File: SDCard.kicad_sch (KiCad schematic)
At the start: 3 parts, among them J1 Micro_SD_Card_Det1, U1 rv1126/rv1109

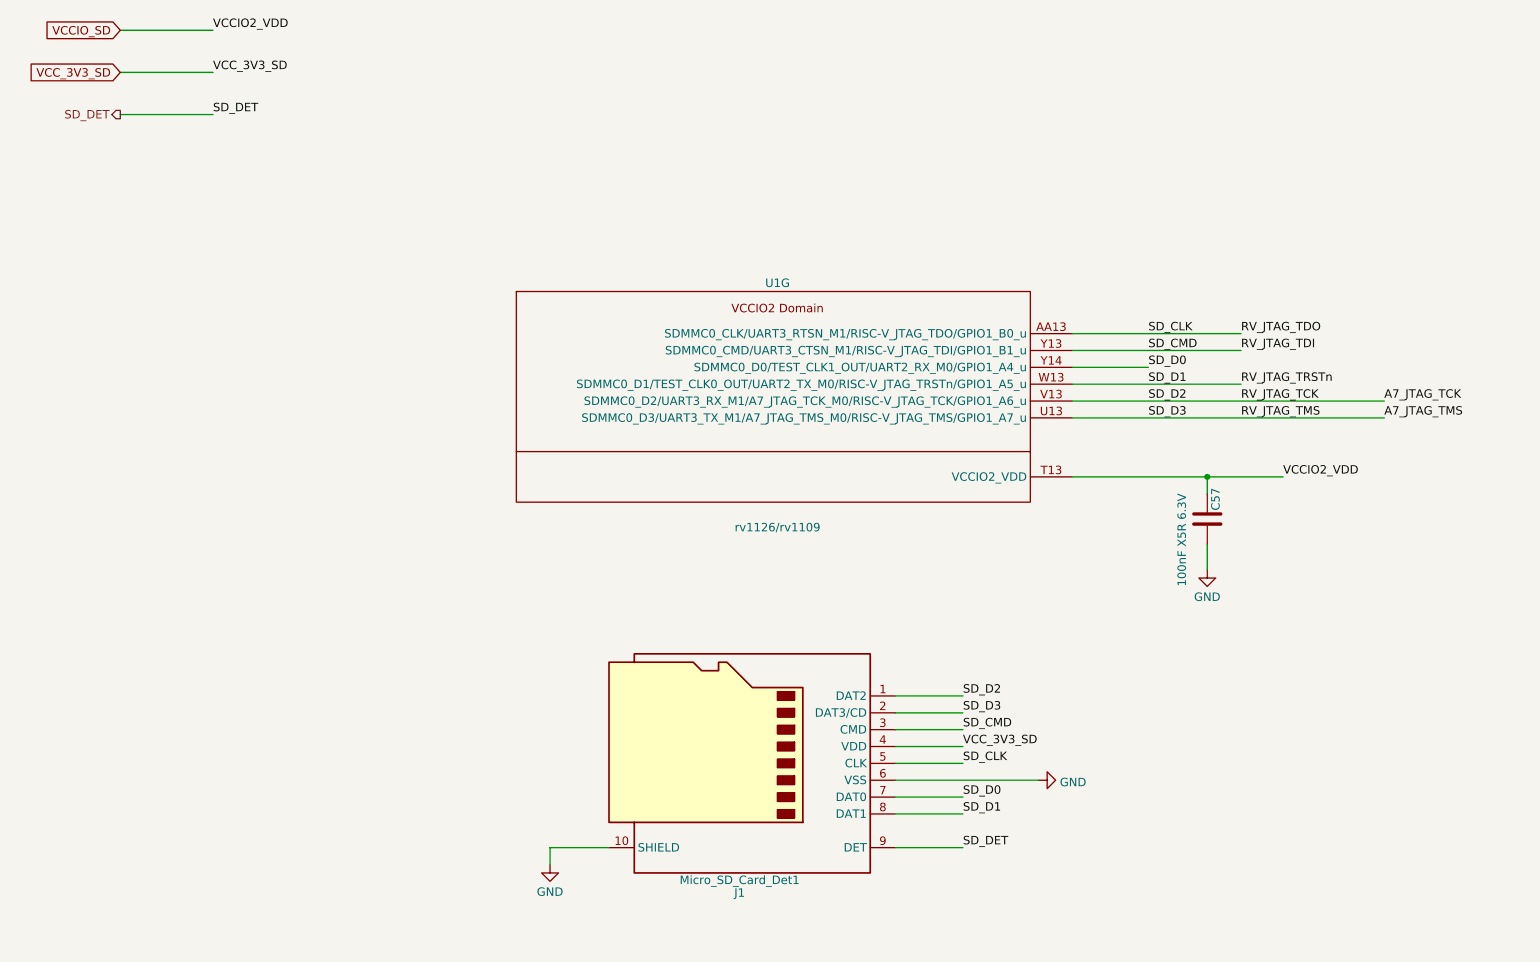
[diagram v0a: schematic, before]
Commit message: added SDCard
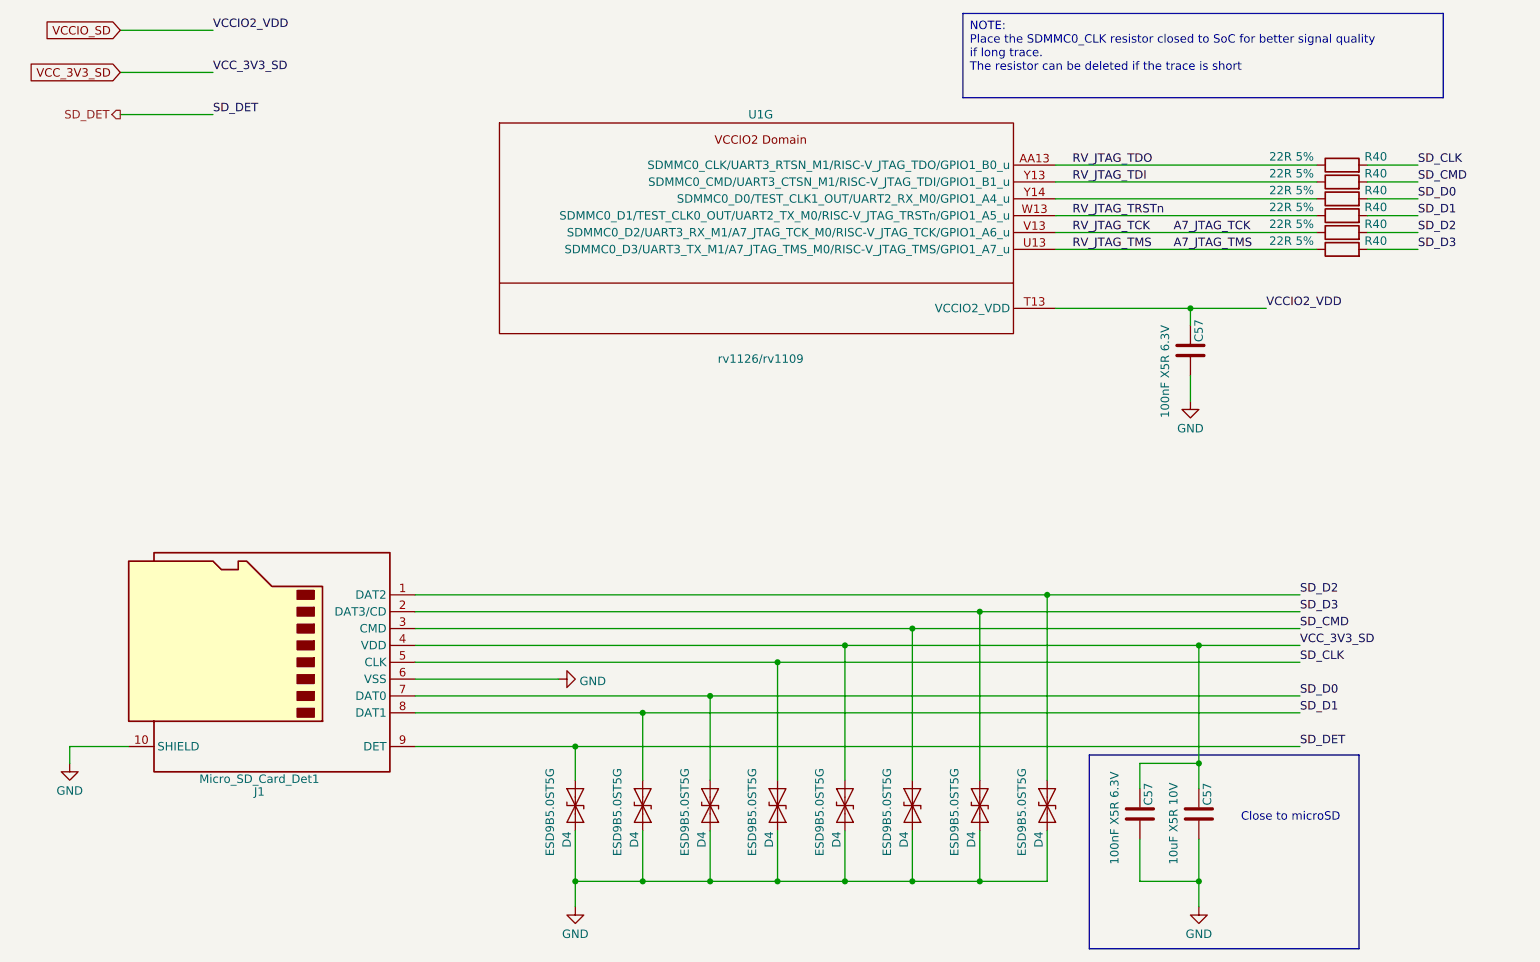
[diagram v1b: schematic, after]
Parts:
- added C57: 10uF X5R 10V, Capacitor_SMD:C_0603_1608Metric, symbol Device:C
- added C57: 100nF X5R 6.3V, Capacitor_SMD:C_0402_1005Metric, symbol Device:C
- added D4 (x8): ESD9B5.0ST5G, Diode_SMD:D_SOD-923, symbol Diode:ESD9B5.0ST5G
- added R40 (x6): 22R 5%, Resistor_SMD:R_0402_1005Metric, symbol Device:R
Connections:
- net A7_JTAG_TCK: now also R40.1; no longer J1.1 (DAT2)
- net A7_JTAG_TMS: now also R40.1; no longer J1.2 (DAT3/CD)
- net GND: now also C57.2, C57.2, D4.2 (A2), D4.2 (A2), D4.2 (A2), D4.2 (A2), D4.2 (A2), D4.2 (A2), D4.2 (A2), D4.2 (A2)
- net RV_JTAG_TDI: now also R40.1; no longer J1.3 (CMD)
- net RV_JTAG_TDO: now also R40.1; no longer J1.5 (CLK)
- net RV_JTAG_TRSTn: now also R40.1; no longer J1.8 (DAT1)
- net SD_D0: now also D4.1 (A1), R40.2; no longer U1.Y14 (SDMMC0_D0/TEST_CLK1_OUT/UART2_RX_M0/GPIO1_A4_u)
- net SD_DET: now also D4.1 (A1)
- net VCC_3V3_SD: now also C57.1, C57.1, D4.1 (A1)
- new net: R40.1, U1.Y14 (SDMMC0_D0/TEST_CLK1_OUT/UART2_RX_M0/GPIO1_A4_u)
- new net SD_CLK: D4.1 (A1), J1.5 (CLK), R40.2
- new net SD_CMD: D4.1 (A1), J1.3 (CMD), R40.2
- new net SD_D1: D4.1 (A1), J1.8 (DAT1), R40.2
- new net SD_D2: D4.1 (A1), J1.1 (DAT2), R40.2
- new net SD_D3: D4.1 (A1), J1.2 (DAT3/CD), R40.2
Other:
- note added: "Close to microSD"
- moved on the sheet: C57, J1, U1G

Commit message: updated footprints
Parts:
- U1: footprint (none) -> Rockchip_SoC:Rockchip_RV1126_FCCSP409LD_14.0x14.0mm
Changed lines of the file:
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@@
         )
         (path "/e3b58043-16a3-43c8-9fad-9c9784eebfa4/4417415c-26f1-4372-988d-9fdf1c116b4b"
-          (reference "C110") (unit 1)
+          (reference "C5") (unit 1)
         )
       )
@@
         )
         (path "/e3b58043-16a3-43c8-9fad-9c9784eebfa4/4417415c-26f1-4372-988d-9fdf1c116b4b"
-          (reference "D10") (unit 1)
+          (reference "D3") (unit 1)
         )
       )
@@
         )
         (path "/e3b58043-16a3-43c8-9fad-9c9784eebfa4/4417415c-26f1-4372-988d-9fdf1c116b4b"
-          (reference "D8") (unit 1)
+          (reference "D1") (unit 1)
         )
       )
@@
         )
         (path "/e3b58043-16a3-43c8-9fad-9c9784eebfa4/4417415c-26f1-4372-988d-9fdf1c116b4b"
-          (reference "C100") (unit 1)
+          (reference "C4") (unit 1)
         )
       )
@@
   (symbol (lib_id "power:GND") (at 193.04 153.67 0) (unit 1)
     (in_bom yes) (on_board yes) (dnp no) (fields_autoplaced)
-    (property "Reference" "#PWR087" (at 193.04 160.02 0)
+    (property "Reference" "#PWR010" (at 193.04 160.02 0)
       (effects (font (size 1.27 1.27)) hide)
     )
@@
       (project "leaf"
         (path "/e3b58043-16a3-43c8-9fad-9c9784eebfa4/4417415c-26f1-4372-988d-9fdf1c116b4b"
-          (reference "#PWR087") (unit 1)
+          (reference "#PWR010") (unit 1)
         )
       )
@@
   (symbol (lib_id "power:GND") (at 96.52 119.38 90) (unit 1)
     (in_bom yes) (on_board yes) (dnp no) (fields_autoplaced)
-    (property "Reference" "#PWR075" (at 102.87 119.38 0)
+    (property "Reference" "#PWR07" (at 102.87 119.38 0)
       (effects (font (size 1.27 1.27)) hide)
     )
@@
       (project "leaf"
         (path "/e3b58043-16a3-43c8-9fad-9c9784eebfa4/4417415c-26f1-4372-988d-9fdf1c116b4b"
-          (reference "#PWR075") (unit 1)
+          (reference "#PWR07") (unit 1)
         )
       )
@@
         )
         (path "/e3b58043-16a3-43c8-9fad-9c9784eebfa4/4417415c-26f1-4372-988d-9fdf1c116b4b"
-          (reference "D12") (unit 1)
+          (reference "D5") (unit 1)
         )
       )
@@
         )
         (path "/e3b58043-16a3-43c8-9fad-9c9784eebfa4/4417415c-26f1-4372-988d-9fdf1c116b4b"
-          (reference "D11") (unit 1)
+          (reference "D4") (unit 1)
         )
       )
@@
         )
         (path "/e3b58043-16a3-43c8-9fad-9c9784eebfa4/4417415c-26f1-4372-988d-9fdf1c116b4b"
-          (reference "C109") (unit 1)
+          (reference "C3") (unit 1)
         )
       )
@@
         )
         (path "/e3b58043-16a3-43c8-9fad-9c9784eebfa4/4417415c-26f1-4372-988d-9fdf1c116b4b"
-          (reference "D13") (unit 1)
+          (reference "D6") (unit 1)
         )
       )
@@
         )
         (path "/e3b58043-16a3-43c8-9fad-9c9784eebfa4/4417415c-26f1-4372-988d-9fdf1c116b4b"
-          (reference "D15") (unit 1)
+          (reference "D8") (unit 1)
         )
       )
@@
         )
         (path "/e3b58043-16a3-43c8-9fad-9c9784eebfa4/4417415c-26f1-4372-988d-9fdf1c116b4b"
-          (reference "R49") (unit 1)
+          (reference "R11") (unit 1)
         )
       )
@@
       (effects (font (size 1.27 1.27)))
     )
-    (property "Footprint" "" (at 144.78 93.98 0)
+    (property "Footprint" "Rockchip_SoC:Rockchip_RV1126_FCCSP409LD_14.0x14.0mm" (at 144.78 93.98 0)
       (effects (font (size 1.27 1.27)) hide)
     )
@@
         )
         (path "/e3b58043-16a3-43c8-9fad-9c9784eebfa4/4417415c-26f1-4372-988d-9fdf1c116b4b"
-          (reference "R46") (unit 1)
+          (reference "R8") (unit 1)
         )
       )
@@
         )
         (path "/e3b58043-16a3-43c8-9fad-9c9784eebfa4/4417415c-26f1-4372-988d-9fdf1c116b4b"
-          (reference "D14") (unit 1)
+          (reference "D7") (unit 1)
         )
       )
@@
         )
         (path "/e3b58043-16a3-43c8-9fad-9c9784eebfa4/4417415c-26f1-4372-988d-9fdf1c116b4b"
-          (reference "D9") (unit 1)
+          (reference "D2") (unit 1)
         )
       )
@@
         )
         (path "/e3b58043-16a3-43c8-9fad-9c9784eebfa4/4417415c-26f1-4372-988d-9fdf1c116b4b"
-          (reference "R48") (unit 1)
+          (reference "R10") (unit 1)
         )
       )
@@
         )
         (path "/e3b58043-16a3-43c8-9fad-9c9784eebfa4/4417415c-26f1-4372-988d-9fdf1c116b4b"
-          (reference "R45") (unit 1)
+          (reference "R7") (unit 1)
         )
       )
@@
   (symbol (lib_id "power:GND") (at 99.06 153.67 0) (unit 1)
     (in_bom yes) (on_board yes) (dnp no) (fields_autoplaced)
-    (property "Reference" "#PWR086" (at 99.06 160.02 0)
+    (property "Reference" "#PWR08" (at 99.06 160.02 0)
       (effects (font (size 1.27 1.27)) hide)
     )
@@
       (project "leaf"
         (path "/e3b58043-16a3-43c8-9fad-9c9784eebfa4/4417415c-26f1-4372-988d-9fdf1c116b4b"
-          (reference "#PWR086") (unit 1)
+          (reference "#PWR08") (unit 1)
         )
       )
@@
   (symbol (lib_id "power:GND") (at 22.86 132.08 0) (unit 1)
     (in_bom yes) (on_board yes) (dnp no) (fields_autoplaced)
-    (property "Reference" "#PWR073" (at 22.86 138.43 0)
+    (property "Reference" "#PWR06" (at 22.86 138.43 0)
       (effects (font (size 1.27 1.27)) hide)
     )
@@
       (project "leaf"
         (path "/e3b58043-16a3-43c8-9fad-9c9784eebfa4/4417415c-26f1-4372-988d-9fdf1c116b4b"
-          (reference "#PWR073") (unit 1)
+          (reference "#PWR06") (unit 1)
         )
       )
@@
         )
         (path "/e3b58043-16a3-43c8-9fad-9c9784eebfa4/4417415c-26f1-4372-988d-9fdf1c116b4b"
-          (reference "R47") (unit 1)
+          (reference "R9") (unit 1)
         )
       )
@@
   (symbol (lib_id "power:GND") (at 191.77 77.47 0) (unit 1)
     (in_bom yes) (on_board yes) (dnp no) (fields_autoplaced)
-    (property "Reference" "#PWR074" (at 191.77 83.82 0)
+    (property "Reference" "#PWR09" (at 191.77 83.82 0)
       (effects (font (size 1.27 1.27)) hide)
     )
@@
       (project "leaf"
         (path "/e3b58043-16a3-43c8-9fad-9c9784eebfa4/4417415c-26f1-4372-988d-9fdf1c116b4b"
-          (reference "#PWR074") (unit 1)
+          (reference "#PWR09") (unit 1)
         )
       )
@@
         )
         (path "/e3b58043-16a3-43c8-9fad-9c9784eebfa4/4417415c-26f1-4372-988d-9fdf1c116b4b"
-          (reference "R44") (unit 1)
-        )
-      )
+          (reference "R6") (unit 1)
+        )
+      )

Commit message: updated Capacitors
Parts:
- C57: LCSC (none) -> C469532; Model (none) -> GRM188B31A106KE69D; Vendor (none) -> muRata(村田)
- C57: LCSC (none) -> C76934; Model (none) -> GRM033R61A104KE15D; Vendor (none) -> muRata(村田)
- C57: footprint Capacitor_SMD:C_0402_1005Metric -> Capacitor_SMD:C_0201_0603Metric; LCSC (none) -> C76934; Model (none) -> GRM033R61A104KE15D; Vendor (none) -> muRata(村田)
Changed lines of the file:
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@@
+      (effects (font (size 1.27 1.27)) hide)
+    )
+    (property "Description" "容值: 10uF 精度: ±10% 额定电压: 10V 材质(温度系数): B B(JIS)" (at 193.04 139.7 0)
+      (effects (font (size 1.27 1.27)) hide)
+    )
+    (property "LCSC" "C469532" (at 193.04 139.7 0)
+      (effects (font (size 1.27 1.27)) hide)
+    )
+    (property "Model" "GRM188B31A106KE69D" (at 193.04 139.7 0)
+      (effects (font (size 1.27 1.27)) hide)
+    )
+    (property "Vendor" "muRata(村田)" (at 193.04 139.7 0)
       (effects (font (size 1.27 1.27)) hide)
     )
@@
     )
     (property "Datasheet" "~" (at 191.77 69.85 0)
+      (effects (font (size 1.27 1.27)) hide)
+    )
+    (property "Description" "容值: 100nF 精度: ±10% 额定电压: 10V 材质(温度系数): X5R 材质:X5R" (at 191.77 69.85 0)
+      (effects (font (size 1.27 1.27)) hide)
+    )
+    (property "LCSC" "C76934" (at 191.77 69.85 0)
+      (effects (font (size 1.27 1.27)) hide)
+    )
+    (property "Model" "GRM033R61A104KE15D" (at 191.77 69.85 0)
+      (effects (font (size 1.27 1.27)) hide)
+    )
+    (property "Vendor" "muRata(村田)" (at 191.77 69.85 0)
       (effects (font (size 1.27 1.27)) hide)
     )
@@
       (effects (font (size 1.27 1.27)) (justify left))
     )
-    (property "Footprint" "Capacitor_SMD:C_0402_1005Metric" (at 185.1152 143.51 0)
+    (property "Footprint" "Capacitor_SMD:C_0201_0603Metric" (at 185.1152 143.51 0)
       (effects (font (size 1.27 1.27)) hide)
     )
@@
       (effects (font (size 1.27 1.27)) hide)
     )
+    (property "Description" "容值: 100nF 精度: ±10% 额定电压: 10V 材质(温度系数): X5R 材质:X5R" (at 184.15 139.7 0)
+      (effects (font (size 1.27 1.27)) hide)
+    )
+    (property "LCSC" "C76934" (at 184.15 139.7 0)
+      (effects (font (size 1.27 1.27)) hide)
+    )
+    (property "Model" "GRM033R61A104KE15D" (at 184.15 139.7 0)
+      (effects (font (size 1.27 1.27)) hide)
+    )
+    (property "Vendor" "muRata(村田)" (at 184.15 139.7 0)
+      (effects (font (size 1.27 1.27)) hide)
+    )

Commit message: updated LCSC selection of capacitors
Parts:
- C57: footprint Capacitor_SMD:C_0603_1608Metric -> Capacitor_SMD:C_0402_1005Metric; LCSC C469532 -> C77000; Model GRM188B31A106KE69D -> GRM155R61A106ME44D
- J1: footprint (none) -> Connector_Card:microSD_HC_Wuerth_693072010801
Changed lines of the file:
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@@
       (effects (font (size 1.27 1.27)) (justify left))
     )
-    (property "Footprint" "Capacitor_SMD:C_0603_1608Metric" (at 194.0052 143.51 0)
+    (property "Footprint" "Capacitor_SMD:C_0402_1005Metric" (at 194.0052 143.51 0)
       (effects (font (size 1.27 1.27)) hide)
     )
@@
       (effects (font (size 1.27 1.27)) hide)
     )
-    (property "Description" "容值: 10uF 精度: ±10% 额定电压: 10V 材质(温度系数): B B(JIS)" (at 193.04 139.7 0)
-      (effects (font (size 1.27 1.27)) hide)
-    )
-    (property "LCSC" "C469532" (at 193.04 139.7 0)
-      (effects (font (size 1.27 1.27)) hide)
-    )
-    (property "Model" "GRM188B31A106KE69D" (at 193.04 139.7 0)
+    (property "Description" "容值: 10uF 精度: ±20% 额定电压: 10V 材质(温度系数): X5R 材质:X5R" (at 193.04 139.7 0)
+      (effects (font (size 1.27 1.27)) hide)
+    )
+    (property "LCSC" "C77000" (at 193.04 139.7 0)
+      (effects (font (size 1.27 1.27)) hide)
+    )
+    (property "Model" "GRM155R61A106ME44D" (at 193.04 139.7 0)
       (effects (font (size 1.27 1.27)) hide)
     )
@@
       (effects (font (size 1.27 1.27)))
     )
-    (property "Footprint" "" (at 0 99.06 0)
-      (effects (font (size 1.27 1.27)) hide)
-    )
+    (property "Footprint" "Connector_Card:microSD_HC_Wuerth_693072010801" (at 0 99.06 0)
+      (effects (font (size 1.27 1.27)) hide)
+    )

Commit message: layout SoC Power and DDR capacitors
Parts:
- C57: LCSC C76934 -> C76928; Model GRM033R61A104KE15D -> GRM033R60J104KE19D
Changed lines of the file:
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@@
       (effects (font (size 1.27 1.27)) hide)
     )
-    (property "Description" "容值: 100nF 精度: ±10% 额定电压: 10V 材质(温度系数): X5R 材质:X5R" (at 191.77 69.85 0)
+    (property "Description" "容值: 100nF 精度: ±10% 额定电压: 6.3V 材质(温度系数): X5R 材质:X5R" (at 191.77 69.85 0)
       (effects (font (size 1.27 1.27)) hide)
     )
-    (property "LCSC" "C76934" (at 191.77 69.85 0)
+    (property "LCSC" "C76928" (at 191.77 69.85 0)
       (effects (font (size 1.27 1.27)) hide)
     )
-    (property "Model" "GRM033R61A104KE15D" (at 191.77 69.85 0)
+    (property "Model" "GRM033R60J104KE19D" (at 191.77 69.85 0)
       (effects (font (size 1.27 1.27)) hide)
     )
@@
       (effects (font (size 1.27 1.27)) hide)
     )
-    (property "Description" "容值: 100nF 精度: ±10% 额定电压: 10V 材质(温度系数): X5R 材质:X5R" (at 184.15 139.7 0)
+    (property "Description" "容值: 100nF 精度: ±10% 额定电压: 6.3V 材质(温度系数): X5R 材质:X5R" (at 184.15 139.7 0)
       (effects (font (size 1.27 1.27)) hide)
     )
-    (property "LCSC" "C76934" (at 184.15 139.7 0)
+    (property "LCSC" "C76928" (at 184.15 139.7 0)
       (effects (font (size 1.27 1.27)) hide)
     )
-    (property "Model" "GRM033R61A104KE15D" (at 184.15 139.7 0)
+    (property "Model" "GRM033R60J104KE19D" (at 184.15 139.7 0)
       (effects (font (size 1.27 1.27)) hide)
     )

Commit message: updated Resistors
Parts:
- R40: LCSC (none) -> C59651; Model (none) -> 0402WGF221JTCE; Vendor (none) -> UNI-ROYAL(厚声)
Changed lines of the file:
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@@
+      (effects (font (size 1.27 1.27)) hide)
+    )
+    (property "Description" "电阻类型: 厚膜电阻 阻值: 22.1Ω 精度: ±1% 功率: 1/16W 温度系数: ±100ppm/℃ 最大工作电压: 50V 工作温度" (at 214.63 54.61 0)
+      (effects (font (size 1.27 1.27)) hide)
+    )
+    (property "LCSC" "C59651" (at 214.63 54.61 0)
+      (effects (font (size 1.27 1.27)) hide)
+    )
+    (property "Model" "0402WGF221JTCE" (at 214.63 54.61 0)
+      (effects (font (size 1.27 1.27)) hide)
+    )
+    (property "Vendor" "UNI-ROYAL(厚声)" (at 214.63 54.61 0)
       (effects (font (size 1.27 1.27)) hide)
     )
@@
       (effects (font (size 1.27 1.27)) hide)
     )
+    (property "Description" "电阻类型: 厚膜电阻 阻值: 22.1Ω 精度: ±1% 功率: 1/16W 温度系数: ±100ppm/℃ 最大工作电压: 50V 工作温度" (at 214.63 46.99 0)
+      (effects (font (size 1.27 1.27)) hide)
+    )
+    (property "LCSC" "C59651" (at 214.63 46.99 0)
+      (effects (font (size 1.27 1.27)) hide)
+    )
+    (property "Model" "0402WGF221JTCE" (at 214.63 46.99 0)
+      (effects (font (size 1.27 1.27)) hide)
+    )
+    (property "Vendor" "UNI-ROYAL(厚声)" (at 214.63 46.99 0)
+      (effects (font (size 1.27 1.27)) hide)
+    )
     (pin "1")
     (pin "2")
@@
       (effects (font (size 1.27 1.27)) hide)
     )
+    (property "Description" "电阻类型: 厚膜电阻 阻值: 22.1Ω 精度: ±1% 功率: 1/16W 温度系数: ±100ppm/℃ 最大工作电压: 50V 工作温度" (at 214.63 52.07 0)
+      (effects (font (size 1.27 1.27)) hide)
+    )
+    (property "LCSC" "C59651" (at 214.63 52.07 0)
+      (effects (font (size 1.27 1.27)) hide)
+    )
+    (property "Model" "0402WGF221JTCE" (at 214.63 52.07 0)
+      (effects (font (size 1.27 1.27)) hide)
+    )
+    (property "Vendor" "UNI-ROYAL(厚声)" (at 214.63 52.07 0)
+      (effects (font (size 1.27 1.27)) hide)
+    )
     (pin "1")
     (pin "2")
@@
       (effects (font (size 1.27 1.27)) hide)
     )
+    (property "Description" "电阻类型: 厚膜电阻 阻值: 22.1Ω 精度: ±1% 功率: 1/16W 温度系数: ±100ppm/℃ 最大工作电压: 50V 工作温度" (at 214.63 44.45 0)
+      (effects (font (size 1.27 1.27)) hide)
+    )
+    (property "LCSC" "C59651" (at 214.63 44.45 0)
+      (effects (font (size 1.27 1.27)) hide)
+    )
+    (property "Model" "0402WGF221JTCE" (at 214.63 44.45 0)
+      (effects (font (size 1.27 1.27)) hide)
+    )
+    (property "Vendor" "UNI-ROYAL(厚声)" (at 214.63 44.45 0)
+      (effects (font (size 1.27 1.27)) hide)
+    )
     (pin "1")
     (pin "2")
@@
       (effects (font (size 1.27 1.27)) hide)
     )
+    (property "Description" "电阻类型: 厚膜电阻 阻值: 22.1Ω 精度: ±1% 功率: 1/16W 温度系数: ±100ppm/℃ 最大工作电压: 50V 工作温度" (at 214.63 49.53 0)
+      (effects (font (size 1.27 1.27)) hide)
+    )
+    (property "LCSC" "C59651" (at 214.63 49.53 0)
+      (effects (font (size 1.27 1.27)) hide)
+    )
+    (property "Model" "0402WGF221JTCE" (at 214.63 49.53 0)
+      (effects (font (size 1.27 1.27)) hide)
+    )
+    (property "Vendor" "UNI-ROYAL(厚声)" (at 214.63 49.53 0)
+      (effects (font (size 1.27 1.27)) hide)
+    )
     (pin "1")
     (pin "2")
@@
       (effects (font (size 1.27 1.27)) hide)
     )
+    (property "Description" "电阻类型: 厚膜电阻 阻值: 22.1Ω 精度: ±1% 功率: 1/16W 温度系数: ±100ppm/℃ 最大工作电压: 50V 工作温度" (at 214.63 41.91 0)
+      (effects (font (size 1.27 1.27)) hide)
+    )
+    (property "LCSC" "C59651" (at 214.63 41.91 0)
+      (effects (font (size 1.27 1.27)) hide)
+    )
+    (property "Model" "0402WGF221JTCE" (at 214.63 41.91 0)
+      (effects (font (size 1.27 1.27)) hide)
+    )
+    (property "Vendor" "UNI-ROYAL(厚声)" (at 214.63 41.91 0)
+      (effects (font (size 1.27 1.27)) hide)
+    )
